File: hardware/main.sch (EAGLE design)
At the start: 100 parts, among them IC1 MPU-6050, IC2 TB6612FNG, M1 MOTOR_MOUNT_V2, M2 LED_MOUNT, M3 LED_MOUNT, M4 LED_MOUNT, M5 LED_MOUNT, M6 LED_MOUNT, M7 LED_MOUNT, Q7 IRLML2244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

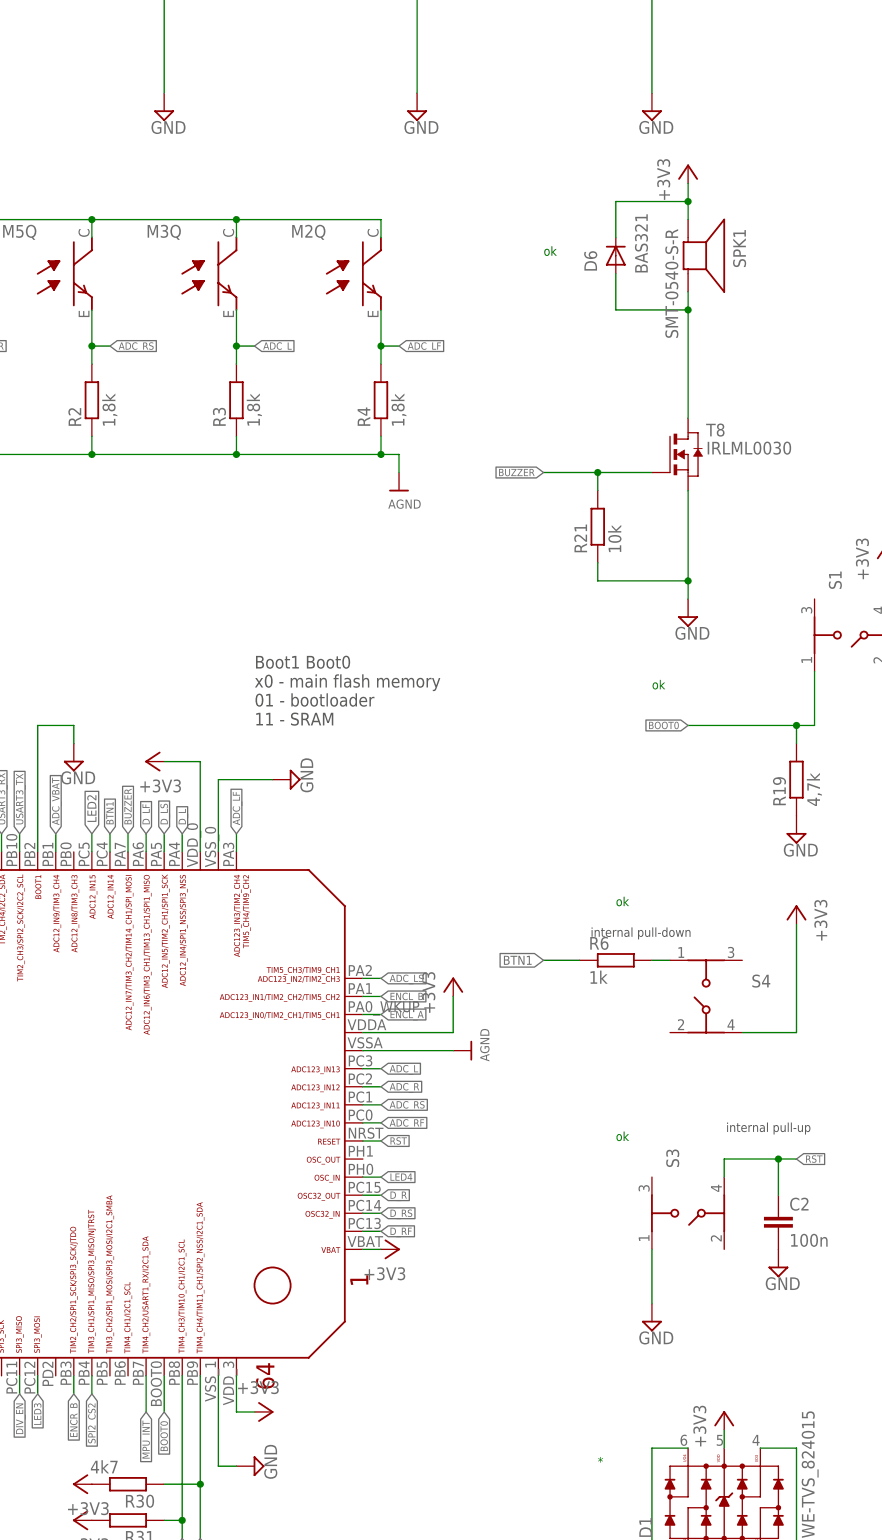
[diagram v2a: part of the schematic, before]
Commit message: fixed boot0 button, buzzer footprint, togh matches 3d model
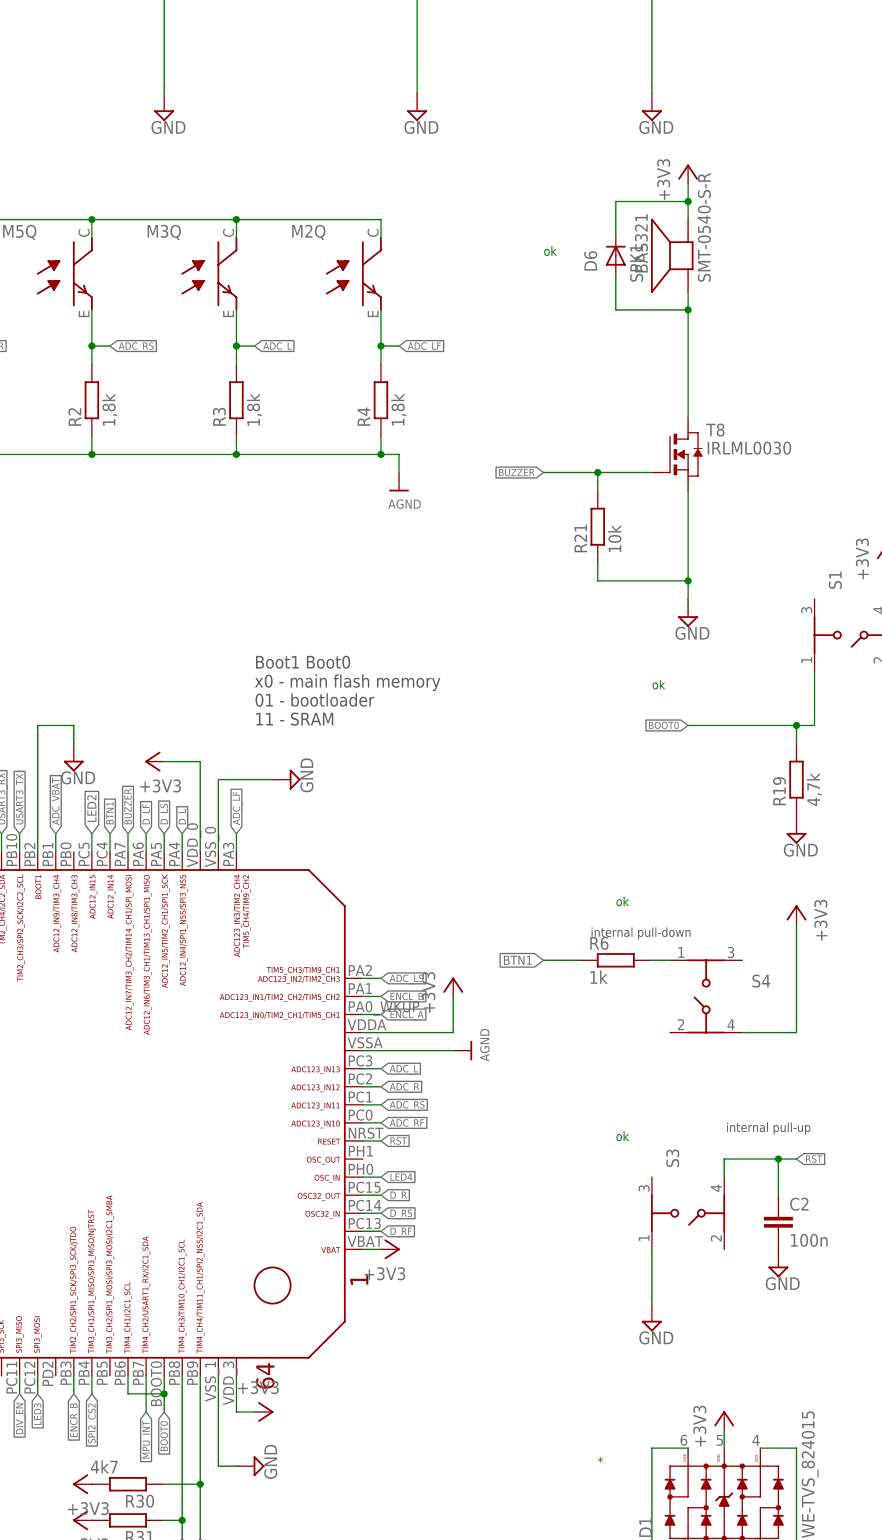
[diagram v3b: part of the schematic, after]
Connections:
- net +3V3: now also SPK1.-; no longer SPK1.+
- net BOOT0: now also U3.PB6
- net N$30: now also SPK1.+; no longer SPK1.-
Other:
- moved on the sheet: SPK1
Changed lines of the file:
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@@
 <instance part="T6" gate="A" x="127" y="210.82"/>
 <instance part="AGND4" gate="GND" x="127" y="187.96"/>
-<instance part="SPK1" gate="G$1" x="132.08" y="167.64" rot="R270"/>
+<instance part="SPK1" gate="G$1" x="132.08" y="167.64" rot="R90"/>
 <instance part="T8" gate="A" x="132.08" y="139.7"/>
 <instance part="AGND12" gate="GND" x="132.08" y="116.84"/>
@@
 </segment>
 <segment>
-<pinref part="SPK1" gate="G$1" pin="+"/>
-<wire x1="132.08" y1="172.72" x2="132.08" y2="175.26" width="0.1524" layer="91"/>
 <pinref part="+3V2" gate="G$1" pin="+3V3"/>
 <pinref part="D6" gate="G$1" pin="K"/>
@@
 <wire x1="121.92" y1="170.18" x2="121.92" y2="175.26" width="0.1524" layer="91"/>
 <wire x1="121.92" y1="175.26" x2="132.08" y2="175.26" width="0.1524" layer="91"/>
+<pinref part="SPK1" gate="G$1" pin="-"/>
+<wire x1="132.08" y1="175.26" x2="132.08" y2="172.72" width="0.1524" layer="91"/>
 <junction x="132.08" y="175.26"/>
 </segment>
@@
 <label x="58.42" y="5.08" size="1.016" layer="95" rot="R270" xref="yes"/>
 <pinref part="U3" gate="G$1" pin="BOOT0"/>
-<wire x1="58.42" y1="10.16" x2="58.42" y2="5.08" width="0.1524" layer="91"/>
+<wire x1="58.42" y1="10.16" x2="58.42" y2="7.62" width="0.1524" layer="91"/>
+<pinref part="U3" gate="G$1" pin="PB6"/>
+<wire x1="58.42" y1="7.62" x2="58.42" y2="5.08" width="0.1524" layer="91"/>
+<wire x1="53.34" y1="10.16" x2="53.34" y2="7.62" width="0.1524" layer="91"/>
+<wire x1="53.34" y1="7.62" x2="58.42" y2="7.62" width="0.1524" layer="91"/>
+<junction x="58.42" y="7.62"/>
 </segment>
 <segment>
@@
 <net name="N$30" class="0">
 <segment>
-<wire x1="132.08" y1="162.56" x2="132.08" y2="160.02" width="0.1524" layer="91"/>
-<pinref part="SPK1" gate="G$1" pin="-"/>
 <wire x1="132.08" y1="160.02" x2="121.92" y2="160.02" width="0.1524" layer="91"/>
-<junction x="132.08" y="160.02"/>
 <pinref part="D6" gate="G$1" pin="A"/>
 <wire x1="121.92" y1="160.02" x2="121.92" y2="165.1" width="0.1524" layer="91"/>
 <pinref part="T8" gate="A" pin="D"/>
 <wire x1="132.08" y1="160.02" x2="132.08" y2="144.78" width="0.1524" layer="91"/>
-</segment>
-</net>
+<pinref part="SPK1" gate="G$1" pin="+"/>
+<wire x1="132.08" y1="160.02" x2="132.08" y2="162.56" width="0.1524" layer="91"/>
+<junction x="132.08" y="160.02"/>
+</segment>
+</net>
